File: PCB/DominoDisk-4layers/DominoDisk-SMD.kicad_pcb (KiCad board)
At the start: 4 copper layers, 45.7 x 32.6 mm, 33 parts, among them J1 Daisy port out, J2 ICSP_ISP6, J3 Daisy port in, J4 UART, K1 TF-104, U1 PC817C-S, U2 SE5218, U3 ATmega328P-AU, U4 TXB0104PWR, Y1 Resonator

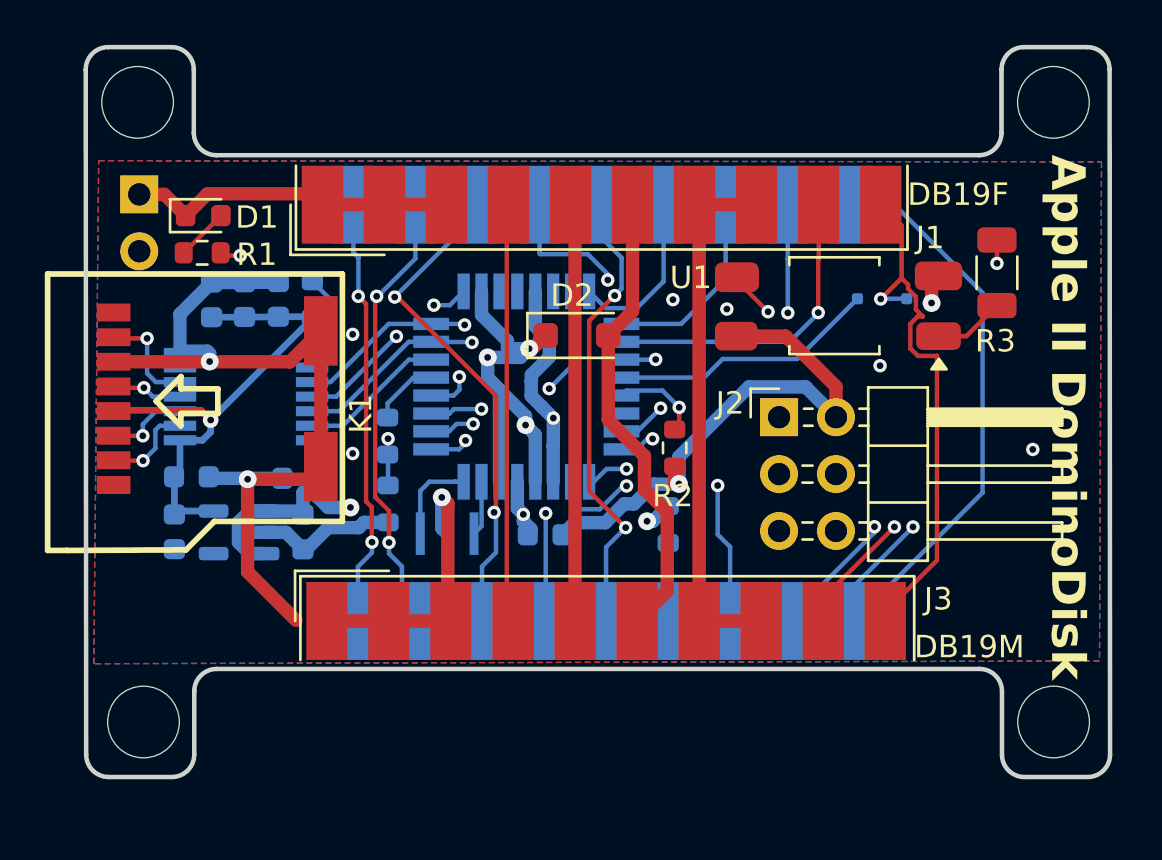
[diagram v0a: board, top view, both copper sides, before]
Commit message: Fix microSD caps
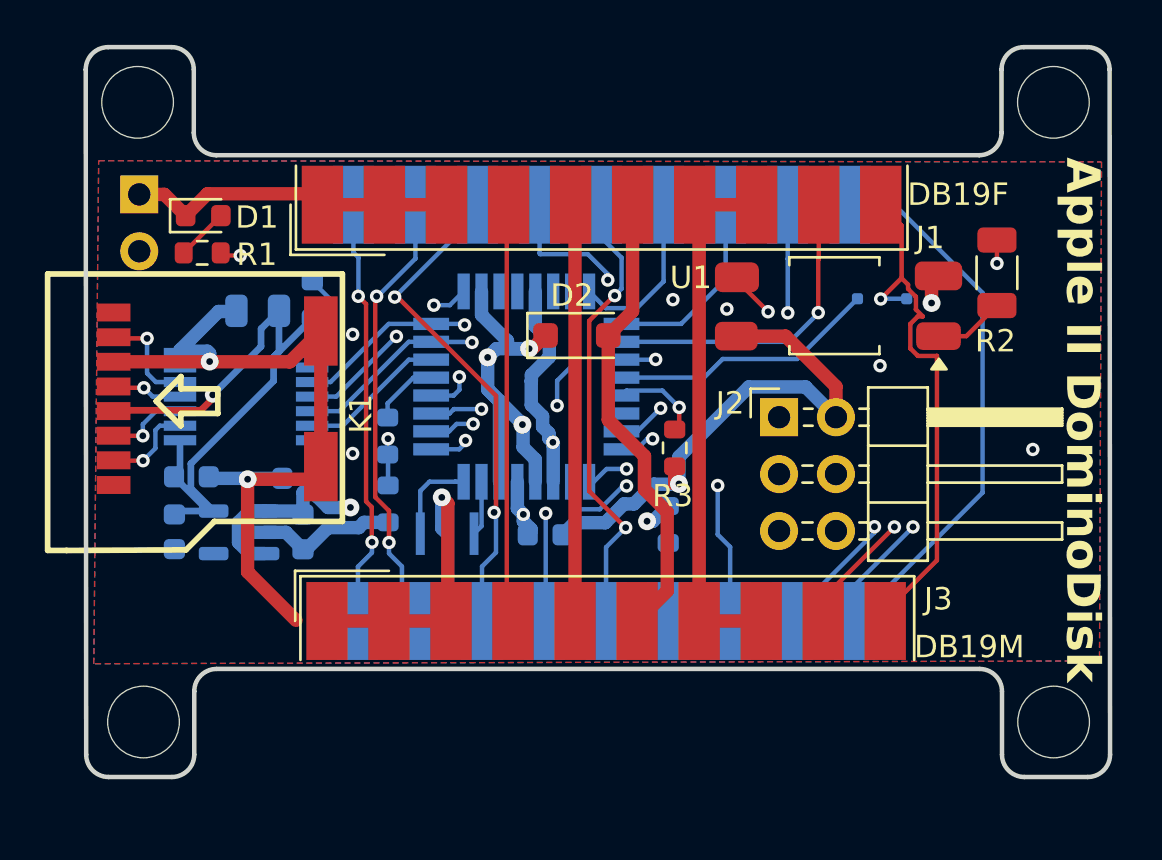
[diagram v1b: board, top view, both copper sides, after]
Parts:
- removed the C1 at (107.7, 50.6)
- removed the C2 at (106.1, 50.6)
- C1: renamed from C3; value 100n -> 22uF; footprint Capacitor_SMD:C_0603_1608Metric -> Capacitor_SMD:C_0805_2012Metric
- moved C1 2.12 mm to (106.7, 51.1), turned to 0 degrees
- renumbered C6 to C2, C7 to C3, C8 to C4, C4 to C5, C5 to C6, R3 to R2, R2 to R3, R7 to R4, R4 to R5, R5 to R7, U3 to U2, U4 to U3, U2 to U4
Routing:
- net 3V3: track 22.0 -> 28.3 mm
- net GND: track 85.7 -> 82.1 mm
- net WRDATA: track 56.5 -> 53.3 mm
- net Net-(R5-Pad2): track 29.0 -> 26.8 mm
- net WREQ: track 20.6 -> 19.1 mm
- net RDDATA: track 45.7 -> 46.9 mm
- net PH1: track 34.1 -> 32.9 mm
- net DRV2_in: track 20.2 -> 19.2 mm
- net TX: track 29.0 -> 28.4 mm
- net -12V: track 19.0 -> 18.4 mm
- removed copper zone on In2.Cu, net GND

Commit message: OCD
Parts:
- C1, C4: moved to F.Cu
- moved C1 12.6 mm to (103.3, 63.2), turned to 180 degrees
- moved C4 4.42 mm to (119.2, 56.7), turned to -90 degrees
- moved R6 1.61 mm to (111.0, 59.5)
- moved K1 1.26 mm to (106.2, 55.0)
- moved Y1 0.89 mm to (116.1, 61.0)
- moved R4 0.76 mm to (108.4, 50.6), turned to 0 degrees
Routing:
- net GND: track 82.1 -> 66.1 mm, vias 13 -> 9
- net 5V_burgerDisk: track 70.5 -> 66.1 mm, vias 5 -> 3
- net WRPROT_out: track 24.0 -> 20.2 mm
- net PH1: track 32.9 -> 36.2 mm
- net PH0: track 35.1 -> 37.6 mm
- net EN3.5: track 18.2 -> 19.9 mm
- net WRDATA: track 53.3 -> 51.8 mm
- net OE: track 3.84 -> 2.36 mm
- net PH2: track 32.4 -> 31.0 mm
- net Net-(U2-XTAL2/PB7): track 4.02 -> 2.74 mm
- net SCLK_L: track 3.07 -> 4.31 mm
- net 3V3: track 28.3 -> 29.5 mm
- net MOSI_L: track 3.72 -> 4.69 mm
- net CS_L: track 4.07 -> 4.86 mm
- net Net-(R5-Pad2): track 26.8 -> 27.5 mm
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- added copper zone on In2.Cu, net GND

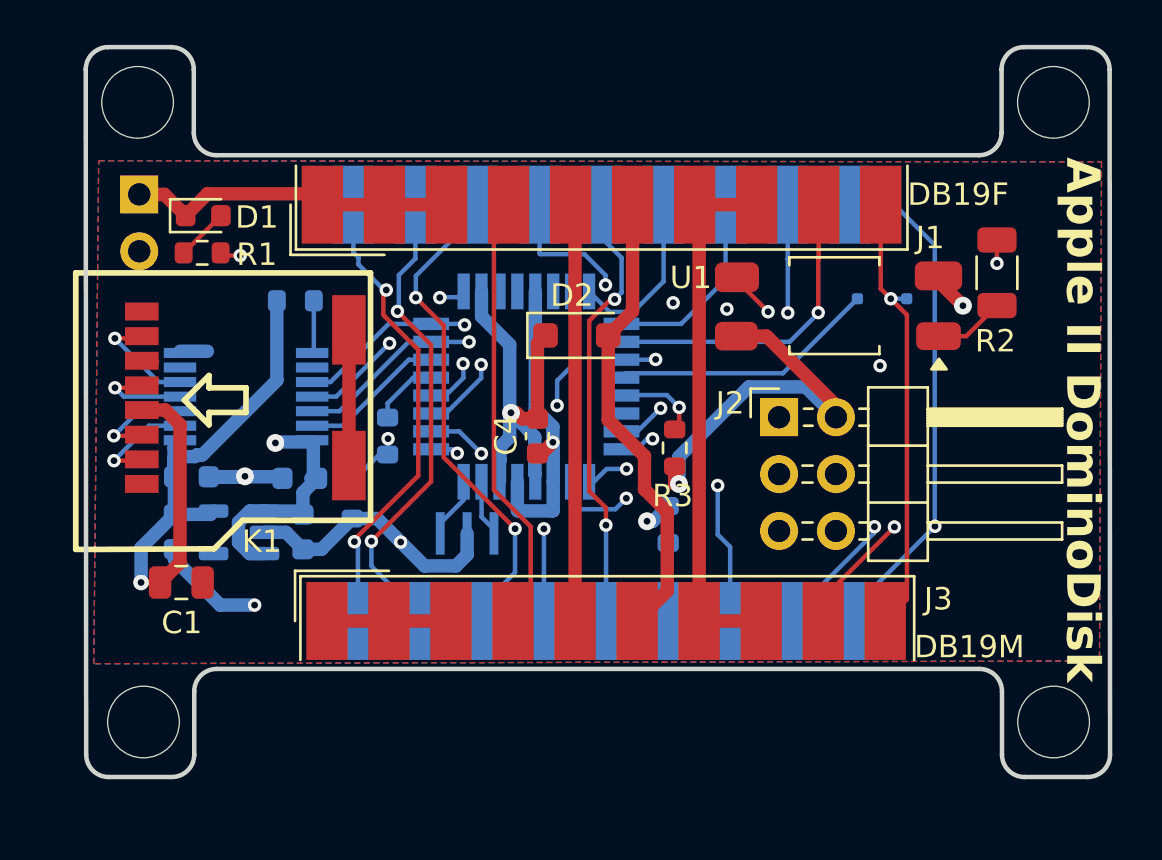
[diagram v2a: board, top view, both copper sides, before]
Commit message: Small caps fixes
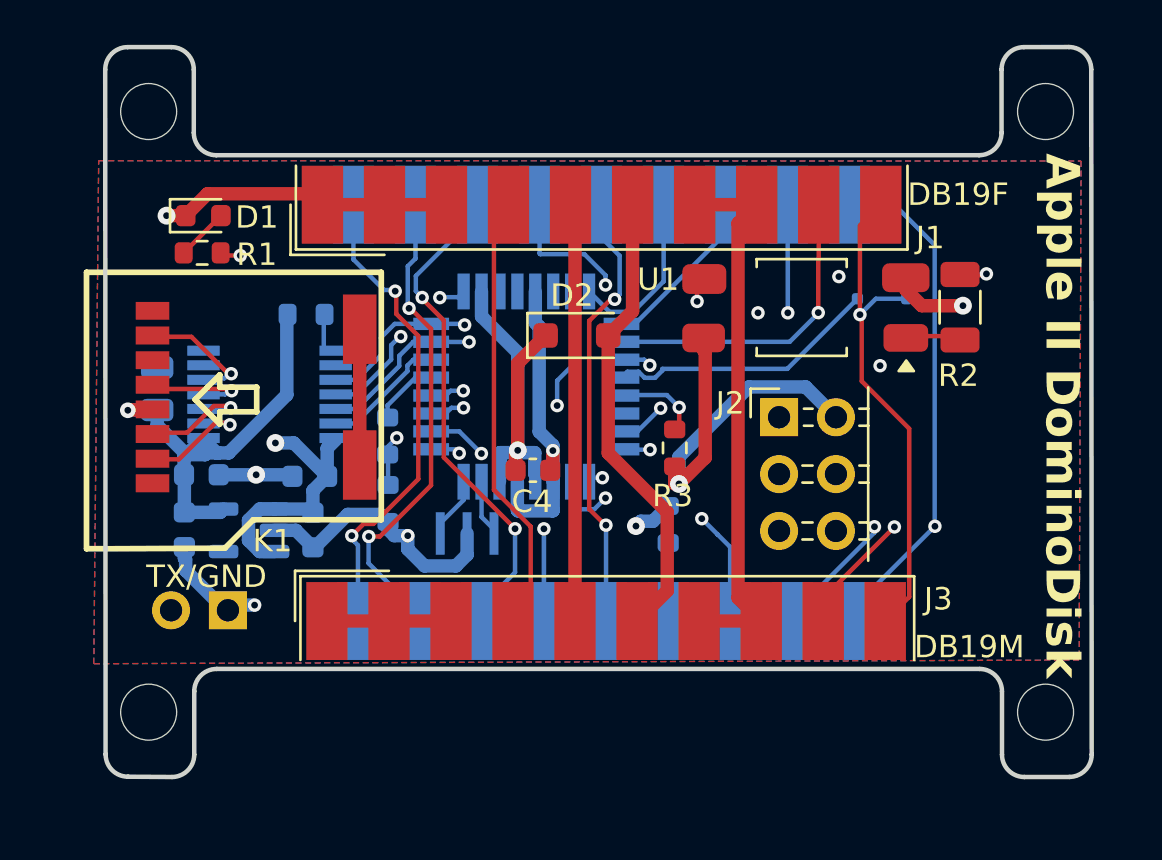
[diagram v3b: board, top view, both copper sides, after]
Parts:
- C1: moved to B.Cu
- J4: footprint Connector_PinHeader_2.54mm:PinHeader_1x02_P2.54mm_Horizontal -> Connector_PinHeader_2.54mm:PinHeader_1x02_P2.54mm_Vertical
- REF**1, REF**2, REF**3, REF**4: value MountingHole_3.2mm_M3 -> MountingHole_2.5mm; footprint MountingHole:MountingHole_3.2mm_M3 -> MountingHole:MountingHole_2.5mm
- moved J4 19.0 mm to (105.4, 64.4), turned to 90 degrees
- moved C1 8.72 mm to (102.2, 54.5), turned to -90 degrees
- moved R2 2.26 mm to (138.1, 50.9)
- moved R6 1.61 mm to (112.5, 59.7)
- moved C4 1.54 mm to (119.0, 58.2), turned to 0 degrees
- moved U1 1.46 mm to (131.0, 50.9)
- moved U3 1.05 mm to (107.3, 54.8)
- moved R4 0.78 mm to (108.9, 51.2)
- moved REF**1 0.64 mm to (101.9, 42.2)
- moved REF**4 0.57 mm to (141.9, 69.0)
- moved REF**2 0.54 mm to (141.9, 42.2)
- moved G*** 0.50 mm to (136.4, 55.8)
- moved REF**3 0.50 mm to (101.9, 69.0)
- moved K1 0.48 mm to (106.7, 54.9)
- moved U4 0.45 mm to (106.3, 60.9)
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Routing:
- net 3V3: track 29.5 -> 20.7 mm
- net TX: track 28.4 -> 35.5 mm
- net Net-(R5-Pad2): track 27.5 -> 22.6 mm
- net 5V_burgerDisk: track 66.1 -> 69.2 mm
- net WRPROT_out: track 20.2 -> 22.7 mm
- net PH1: track 36.2 -> 33.8 mm
- net GND: track 66.1 -> 63.9 mm, vias 9 -> 10
- net PH2: track 31.0 -> 29.2 mm
- net WRDATA: track 51.8 -> 50.4 mm
- net DRV1_out: track 8.14 -> 6.93 mm
- net +12V: track 23.9 -> 24.9 mm
- net CS: track 6.54 -> 5.59 mm
- net MOSI: track 26.9 -> 26.1 mm
- net SCK: track 27.1 -> 26.3 mm
- net SCLK_L: track 4.31 -> 4.96 mm
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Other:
- board size 45.7 x 32.6 mm -> 44 x 32.6 mm
- board text added: "TX/GND"

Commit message: fatter traces
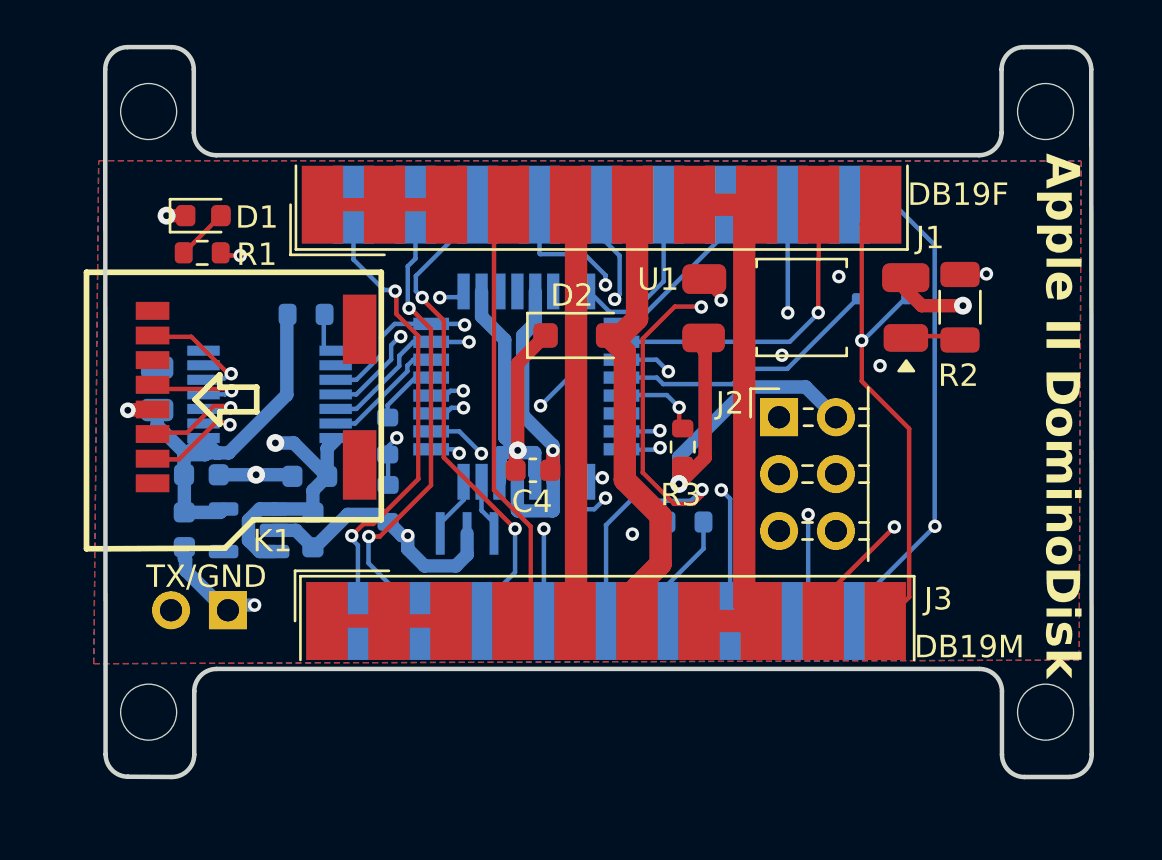
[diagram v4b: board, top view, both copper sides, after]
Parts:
- moved R7 0.76 mm to (125.8, 60.5), turned to 0 degrees
- moved R3 0.36 mm to (125.7, 57.1)
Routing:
- net GND: track 63.9 -> 50.2 mm
- net WREQ: track 18.4 -> 29.3 mm, vias 2 -> 3
- net TX: track 35.5 -> 27.1 mm
- net RDDATA: track 46.2 -> 39.7 mm
- net LED: track 22.4 -> 24.3 mm
- net HDSEL_in: track 3.49 -> 5.07 mm
- net DRV1_in: track 20.3 -> 21.8 mm
- net Net-(R5-Pad2): track 22.6 -> 23.7 mm
- net PH0: track 37.3 -> 38.3 mm
